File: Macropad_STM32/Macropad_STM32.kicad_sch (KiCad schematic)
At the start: 70 parts, among them J1 USB_C_Receptacle_USB2.0, J10 Encoders + LED, J2 Conn_01x04_Pin, J3 JTAG, J7 Power Connector, J9 Matrix, SW1 SW_Push, U1 STM32F103C8T6, U3 AMS1117-3.3, Y1 16MHz

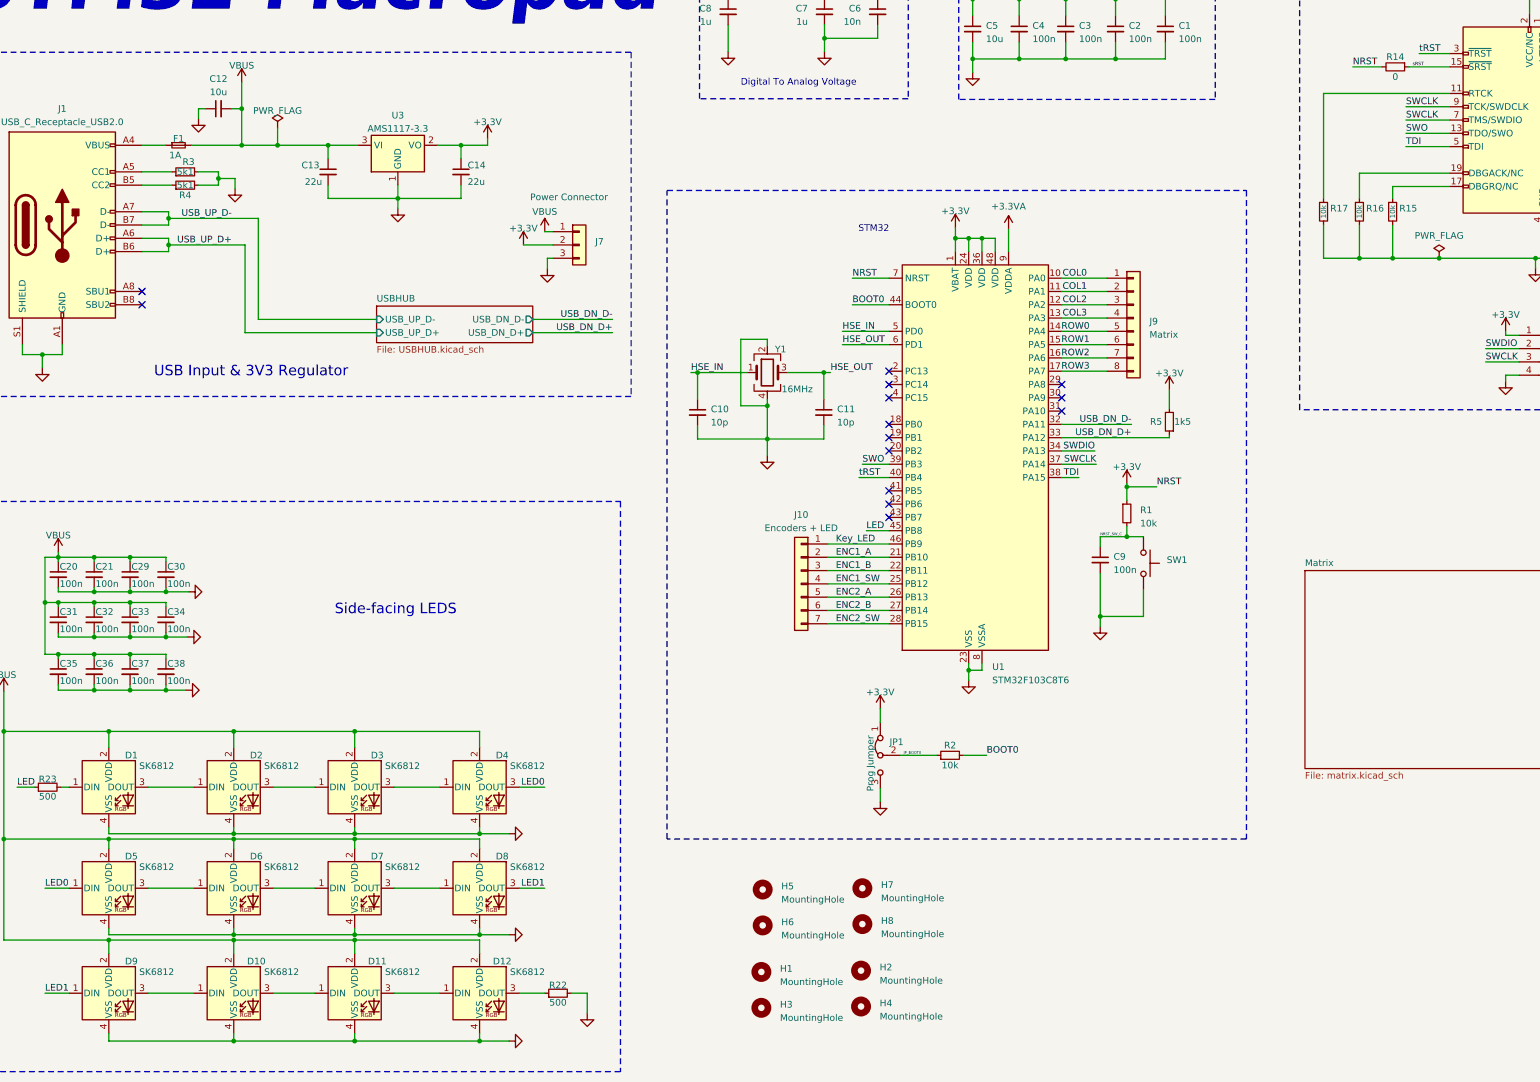
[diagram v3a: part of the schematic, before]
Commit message: Finished PCB layout, TODO: traces
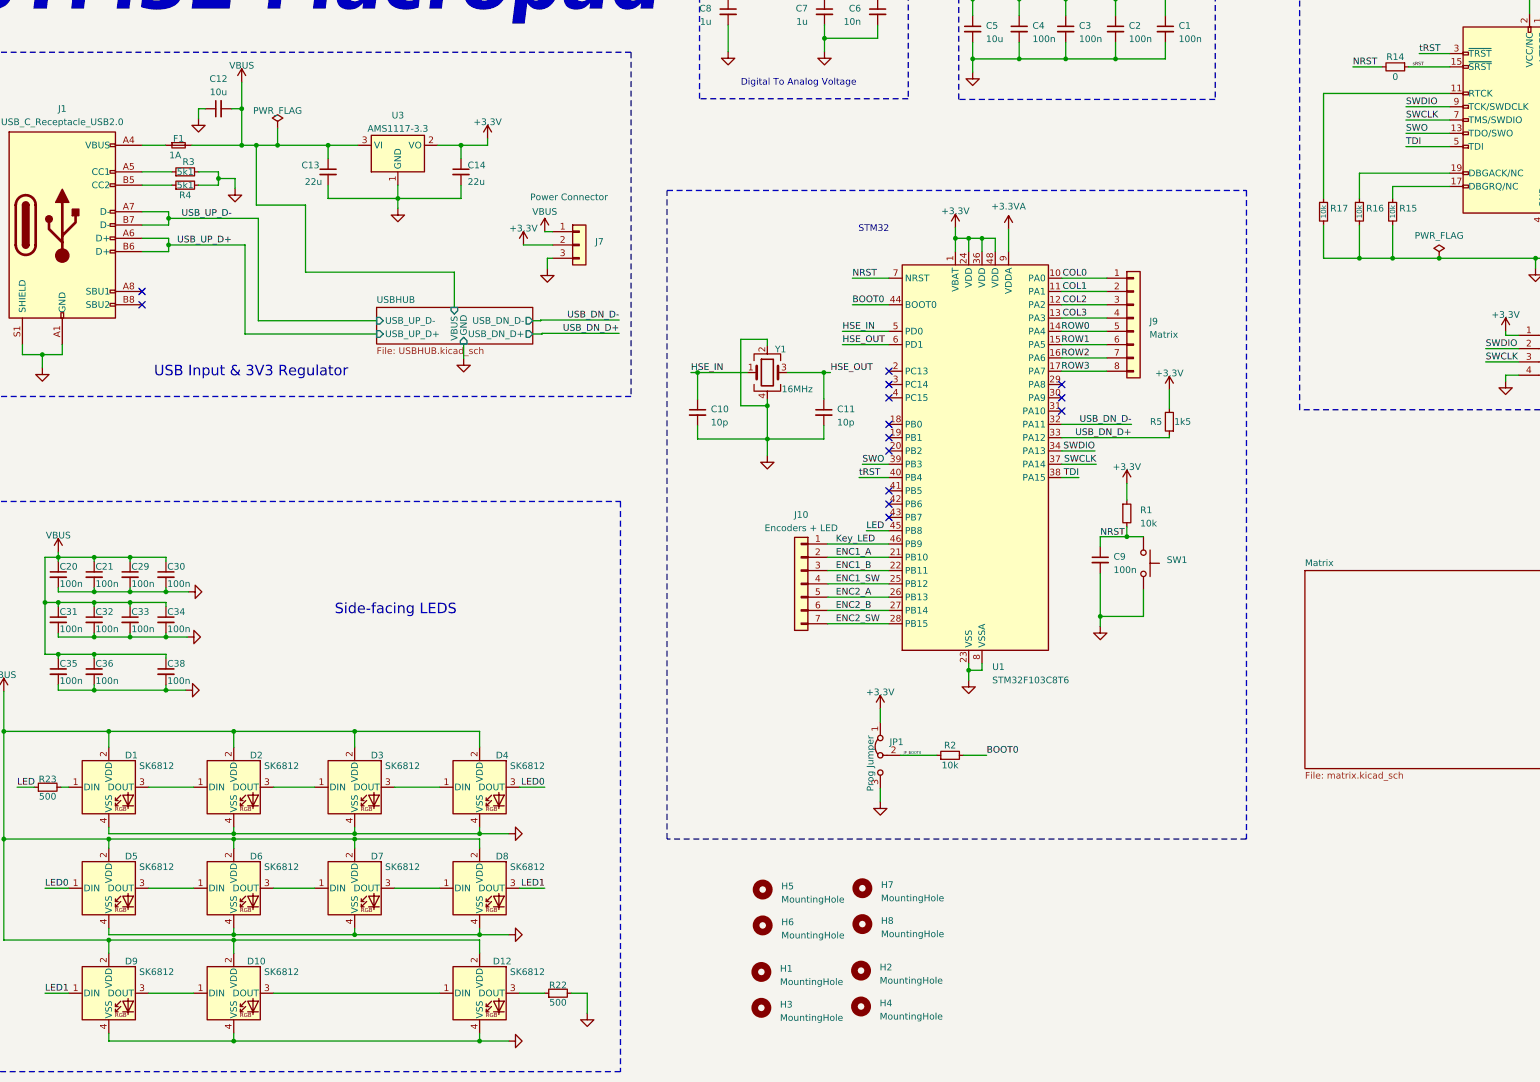
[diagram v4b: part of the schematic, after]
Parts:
- removed C37: 100n, Capacitor_SMD:C_0805_2012Metric_Pad1.18x1.45mm_HandSolder, symbol Device:C_Small
- removed D11: SK6812, SK6812SIDE:SK6812SIDE, symbol LED:SK6812
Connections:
- net +3.3V: no longer R14.2, U1.7 (NRST)
- net SWCLK: no longer J3.9 (TCK/SWDCLK)
- net SWDIO: now also J3.9 (TCK/SWDCLK)
- net at D12.1 (DIN): now also D10.3 (DOUT)
- net NRST_SW_C renamed NRST
- net NRST: now also R14.2, U1.7 (NRST)
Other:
- sheet USBHUB ports: added GND, VBUS; removed none

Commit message: Schematic changes Motherboard nearing completion
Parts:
- added C17: 100n, Capacitor_SMD:C_0805_2012Metric_Pad1.18x1.45mm_HandSolder, symbol Device:C_Small
- added D11: SK6812, SK6812SIDE:SK6812SIDE, symbol LED:SK6812
- added J18 (x2): Conn_01x04_Socket, Connector_PinHeader_2.54mm:PinHeader_1x04_P2.54mm_Vertical, symbol Connector:Conn_01x04_Socket
- added J21: Matrix, Connector_JST:JST_EH_B8B-EH-A_1x08_P2.50mm_Vertical, symbol Connector_Generic:Conn_01x08
- added J22: Encoders + LED, Connector_JST:JST_EH_B7B-EH-A_1x07_P2.50mm_Vertical, symbol Connector_Generic:Conn_01x07
- added U4: USBLC6-2SC6, Package_TO_SOT_SMD:SOT-23-6, symbol Hub16-rescue:USBLC6-2SC6-josh-ic
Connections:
- net GND: now also C17.2, D11.4 (VSS), J18.4 (Pin_4); no longer J1.A1 (GND), J1.A12 (GND), J1.B1 (GND), J1.B12 (GND), J1.S1 (SHIELD)
- net LED: now also U1.2 (PC13); no longer U1.45 (PB8)
- net USB_UP_D+: now also U4.4 (IO2)
- net USB_UP_D-: now also U4.6 (IO1)
- net VBUS: now also C17.1, D11.2 (VDD), J18.1 (Pin_1); no longer C12.2, F1.2
- net at D10.3 (DOUT): now also D11.1 (DIN); no longer D12.1 (DIN)
- new net: D11.3 (DOUT), D12.1 (DIN)
- new net Matrix/COL0: J21.1 (Pin_1)
- new net Matrix/COL1: J21.2 (Pin_2)
- new net Matrix/COL2: J21.3 (Pin_3)
- new net Matrix/COL3: J21.4 (Pin_4)
- new net Matrix/ENC1_A: J22.2 (Pin_2)
- new net Matrix/ENC1_B: J22.3 (Pin_3)
- new net Matrix/ENC1_SW: J22.4 (Pin_4)
- new net Matrix/ENC2_A: J22.5 (Pin_5)
- new net Matrix/ENC2_B: J22.6 (Pin_6)
- new net Matrix/ENC2_SW: J22.7 (Pin_7)
- new net Matrix/Key_LED: J22.1 (Pin_1)
- new net Matrix/ROW0: J21.5 (Pin_5)
- new net Matrix/ROW1: J21.6 (Pin_6)
- new net Matrix/ROW2: J21.7 (Pin_7)
- new net Matrix/ROW3: J21.8 (Pin_8)
- new net UP_USB_D+: J18.3 (Pin_3), J18.3 (Pin_3), U4.3 (IO2)
- new net UP_USB_D-: J18.2 (Pin_2), J18.2 (Pin_2), U4.1 (IO1)
- new net USB_UP_GND: J1.A1 (GND), J1.A12 (GND), J1.B1 (GND), J1.B12 (GND), J1.S1 (SHIELD), J18.4 (Pin_4), U4.2 (GND)
- new net VBUS_IN: C12.2, F1.2, J18.1 (Pin_1), U4.5 (VBUS)
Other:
- sheet Matrix ports: added COL0, COL1, COL2, COL3, ENC1_A, ENC1_B, ENC1_SW, ENC2_A, ENC2_B, ENC2_SW, Key_LED, ROW0, ROW1, ROW2, ROW3; removed none
- sheet USBHUB ports: added UP_USB_D+, UP_USB_D-; removed USB_UP_D+, USB_UP_D-
- company: (none) -> Irfaan
- moved on the sheet: C1, C13, C14, C29, C3, C33, C4, C5, C6, C7, C8, C9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

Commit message: Revision 1 nearly finished
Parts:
- removed J2: Conn_01x04_Pin, Connector_PinHeader_2.54mm:PinHeader_1x04_P2.54mm_Vertical, symbol Connector:Conn_01x04_Pin
- added H10, H11, H12, H13, H14, H15, H16, H9: MountingHole, MountingHole:MountingHole_2.2mm_M2, symbol Mechanical:MountingHole
- J18: footprint Connector_PinHeader_2.54mm:PinHeader_1x04_P2.54mm_Vertical -> SK6812SIDE:MOLEX_0781710004
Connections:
- net COL0: now also J9.4 (Pin_4), U1.13 (PA3); no longer J9.1 (Pin_1), U1.10 (PA0)
- net COL1: now also J9.3 (Pin_3), U1.12 (PA2); no longer J9.2 (Pin_2), U1.11 (PA1)
- net COL2: now also J9.2 (Pin_2), U1.11 (PA1); no longer J9.3 (Pin_3), U1.12 (PA2)
- net COL3: now also J9.1 (Pin_1), U1.10 (PA0); no longer J9.4 (Pin_4), U1.13 (PA3)
- net GND: no longer C12.1, R3.2, R4.2
- net Key_LED: now also U1.18 (PB0); no longer U1.46 (PB9)
- net Matrix/COL0: now also J21.4 (Pin_4); no longer J21.1 (Pin_1)
- net Matrix/COL1: now also J21.3 (Pin_3); no longer J21.2 (Pin_2)
- net Matrix/COL2: now also J21.2 (Pin_2); no longer J21.3 (Pin_3)
- net Matrix/COL3: now also J21.1 (Pin_1); no longer J21.4 (Pin_4)
- net USB_UP_GND: now also C12.1, R3.2, R4.2

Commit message: Nearly finished Todo: - Fix silkscreen - Final check
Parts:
- removed H11, H12, H13, H14, H15, H16: MountingHole, MountingHole:MountingHole_2.2mm_M2, symbol Mechanical:MountingHole
- removed H5, H7: MountingHole, MountingHole:MountingHole_3.2mm_M3_DIN965, symbol Mechanical:MountingHole
- removed J10, J22: Encoders + LED, Connector_JST:JST_EH_B7B-EH-A_1x07_P2.50mm_Vertical, symbol Connector_Generic:Conn_01x07
- removed J18 (x2): Conn_01x04_Socket, SK6812SIDE:MOLEX_0781710004, symbol Connector:Conn_01x04_Socket
- removed J21, J9: Matrix, Connector_JST:JST_EH_B8B-EH-A_1x08_P2.50mm_Vertical, symbol Connector_Generic:Conn_01x08
- added J11, J15: 533981571, Connector_Molex:Molex_PicoBlade_53261-1571_1x15-1MP_P1.25mm_Horizontal, symbol 533981571:533981571
- added J18: Conn_01x02_Socket, Connector_PinHeader_2.54mm:PinHeader_1x02_P2.54mm_Vertical, symbol Connector:Conn_01x02_Socket
- JP1: footprint Connector_PinHeader_2.54mm:PinHeader_1x03_P2.54mm_Vertical -> Jumper:SolderJumper-3_P2.0mm_Open_TrianglePad1.0x1.5mm_NumberLabels
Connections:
- net USB_UP_GND is gone; now on net GND: C12.1, J1.A1 (GND), J1.A12 (GND), J1.B1 (GND), J1.B12 (GND), J1.S1 (SHIELD), R3.2, R4.2, U4.2 (GND)
- net VBUS_IN is gone; now on net VBUS: C12.2, F1.2, U4.5 (VBUS)
- net COL0: now also J11.4
- net COL1: now also J11.3
- net COL2: now also J11.2
- net COL3: now also J11.1
- net ENC1_A: now also J11.10
- net ENC1_B: now also J11.11
- net ENC1_SW: now also J11.12
- net ENC2_A: now also J11.13
- net ENC2_B: now also J11.14
- net ENC2_SW: now also J11.15
- net GND: now also J11.S1 (SHIELD1), J11.S2 (SHIELD2), J15.S1 (SHIELD1), J15.S2 (SHIELD2)
- net Key_LED: now also J11.9
- net Matrix/COL0: now also J15.4
- net Matrix/COL1: now also J15.3
- net Matrix/COL2: now also J15.2
- net Matrix/COL3: now also J15.1
- net Matrix/ENC1_A: now also J15.10
- net Matrix/ENC1_B: now also J15.11
- net Matrix/ENC1_SW: now also J15.12
- net Matrix/ENC2_A: now also J15.13
- net Matrix/ENC2_B: now also J15.14
- net Matrix/ENC2_SW: now also J15.15
- net Matrix/Key_LED: now also J15.9
- net Matrix/ROW0: now also J15.5
- net Matrix/ROW1: now also J15.6
- net Matrix/ROW2: now also J15.7
- net Matrix/ROW3: now also J15.8
- net ROW0: now also J11.5
- net ROW1: now also J11.6
- net ROW2: now also J11.7
- net ROW3: now also J11.8
- net UP_USB_D+: now also U4.1 (IO1); no longer U4.3 (IO2)
- net UP_USB_D-: now also U4.3 (IO2); no longer U4.1 (IO1)
- net USB_UP_D+: now also U4.6 (IO1); no longer U4.4 (IO2)
- net USB_UP_D-: now also U4.4 (IO2); no longer U4.6 (IO1)
- net at U1.30 (PA9): now also J18.1 (Pin_1)
- net at U1.31 (PA10): now also J18.2 (Pin_2)
- no-connect marks 14 -> 12
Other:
- moved on the sheet: C1, C10, C11, C13, C14, C2, C3, C4, C5, C6, C7, C8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

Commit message: Hardware finished and motherboard has been tested. Todo: Test keyboard matrix and write firmware.
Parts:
- removed H10, H9: MountingHole, MountingHole:MountingHole_2.2mm_M2, symbol Mechanical:MountingHole
- removed H2, H8: MountingHole, MountingHole:MountingHole_3.2mm_M3_DIN965, symbol Mechanical:MountingHole
- removed J3: JTAG, Connector_PinHeader_2.54mm:PinHeader_2x10_P2.54mm_Vertical, symbol Connector:Conn_ARM_JTAG_SWD_20
- removed R14: 0, Resistor_SMD:R_0805_2012Metric_Pad1.20x1.40mm_HandSolder, symbol Device:R_Small
- removed R15, R16, R17: 10k, Resistor_SMD:R_0805_2012Metric_Pad1.20x1.40mm_HandSolder, symbol Device:R_Small
- removed U1: STM32F103C8T6, Package_QFP:LQFP-48_7x7mm_P0.5mm, symbol MCU_ST_STM32F1:STM32F103C8Tx
- added J4: Conn_ARM_SWD_TagConnect_TC2030, Connector:Tag-Connect_TC2030-IDC-FP_2x03_P1.27mm_Vertical, symbol Connector:Conn_ARM_SWD_TagConnect_TC2030
- added U5: STM32F103C6Ux, Package_DFN_QFN:QFN-48-1EP_7x7mm_P0.5mm_EP5.6x5.6mm, symbol MCU_ST_STM32F1:STM32F103C6Ux
- BOOT JP1: renamed from JP1; footprint Jumper:SolderJumper-3_P2.0mm_Open_TrianglePad1.0x1.5mm_NumberLabels -> Connector_PinHeader_2.54mm:PinHeader_1x03_P2.54mm_Vertical
- Matrix Connector1: renamed from J11; footprint Connector_Molex:Molex_PicoBlade_53261-1571_1x15-1MP_P1.25mm_Horizontal -> Connector_Molex:Molex_PicoBlade_53398-1571_1x15-1MP_P1.25mm_Vertical
- Motherboard Connector1: renamed from J15; footprint Connector_Molex:Molex_PicoBlade_53261-1571_1x15-1MP_P1.25mm_Horizontal -> Connector_Molex:Molex_PicoBlade_53398-1571_1x15-1MP_P1.25mm_Vertical
- TX RX1: renamed from J18
- renumbered J1 to J3, J7 to POWER1, SW1 to RESET1
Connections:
- net +3.3V: now also J4.1 (VCC), U5.1 (VBAT), U5.24 (VDD), U5.36 (VDD), U5.48 (VDD)
- net +3.3VA: now also U5.9 (VDDA)
- net BOOT0: now also U5.44 (BOOT0)
- net COL0: now also Matrix Connector1.7, U5.16 (PA6); no longer Matrix Connector1.4
- net COL1: now also Matrix Connector1.6, U5.15 (PA5); no longer Matrix Connector1.3
- net COL2: now also Matrix Connector1.5, U5.14 (PA4); no longer Matrix Connector1.2
- net COL3: now also Matrix Connector1.4, U5.13 (PA3); no longer Matrix Connector1.1
- net ENC1_A: now also Matrix Connector1.1, U5.10 (PA0); no longer Matrix Connector1.10
- net ENC1_B: now also Matrix Connector1.2, U5.11 (PA1); no longer Matrix Connector1.11
- net ENC1_SW: now also Matrix Connector1.3, U5.12 (PA2); no longer Matrix Connector1.12
- net ENC2_A: now also U5.26 (PB13)
- net ENC2_B: now also U5.27 (PB14)
- net ENC2_SW: now also U5.28 (PB15)
- net GND: now also J4.5 (GND), U5.23 (VSS), U5.35 (VSS), U5.47 (VSS), U5.49 (VSS), U5.8 (VSSA)
- net HSE_IN: now also U5.5 (PD0)
- net HSE_OUT: now also U5.6 (PD1)
- net Key_LED: now also Matrix Connector1.12, U5.25 (PB12); no longer Matrix Connector1.9
- net LED: now also U5.2 (PC13)
- net Matrix/COL0: now also Motherboard Connector1.7; no longer Motherboard Connector1.4
- net Matrix/COL1: now also Motherboard Connector1.6; no longer Motherboard Connector1.3
- net Matrix/COL2: now also Motherboard Connector1.5; no longer Motherboard Connector1.2
- net Matrix/COL3: now also Motherboard Connector1.4; no longer Motherboard Connector1.1
- net Matrix/ENC1_A: now also Motherboard Connector1.1; no longer Motherboard Connector1.10
- net Matrix/ENC1_B: now also Motherboard Connector1.2; no longer Motherboard Connector1.11
- net Matrix/ENC1_SW: now also Motherboard Connector1.3; no longer Motherboard Connector1.12
- net Matrix/Key_LED: now also Motherboard Connector1.12; no longer Motherboard Connector1.9
- net Matrix/ROW0: now also Motherboard Connector1.8; no longer Motherboard Connector1.5
- net Matrix/ROW1: now also Motherboard Connector1.9; no longer Motherboard Connector1.6
- net Matrix/ROW2: now also Motherboard Connector1.10; no longer Motherboard Connector1.7
- net Matrix/ROW3: now also Motherboard Connector1.11; no longer Motherboard Connector1.8
- net NRST: now also J4.3 (~{RESET}), U5.7 (NRST)
- net ROW0: now also Matrix Connector1.8, U5.17 (PA7); no longer Matrix Connector1.5
- net ROW1: now also Matrix Connector1.9, U5.18 (PB0); no longer Matrix Connector1.6
- net ROW2: now also Matrix Connector1.10, U5.21 (PB10); no longer Matrix Connector1.7
- net ROW3: now also Matrix Connector1.11, U5.22 (PB11); no longer Matrix Connector1.8
- net SWCLK: now also J4.4 (SWCLK), U5.37 (PA14)
- net SWDIO: now also J4.2 (SWDIO), U5.34 (PA13)
- net SWO: now also J4.6 (SWO), U5.39 (PB3)
- net TDI: now also U5.38 (PA15)
- net USB_DN_D+: now also U5.33 (PA12)
- net USB_DN_D-: now also U5.32 (PA11)
- net tRST: now also U5.40 (PB4)
- net at TX RX1.1 (Pin_1): now also U5.30 (PA9)
- net at TX RX1.2 (Pin_2): now also U5.31 (PA10)
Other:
- moved on the sheet: C13, C14, C6, C7, C8, FB1, POWER1, U3
